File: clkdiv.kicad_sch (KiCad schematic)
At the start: 58 parts, among them J1 Conn_02x05_Odd_Even, J10 Conn_01x03_Pin, J11 Conn_01x03_Socket, J12 Conn_01x03_Pin, J13 Conn_01x03_Socket, J14 Conn_01x03_Pin, J15 Conn_01x03_Socket, J2 AudioJack2_SwitchT, J3 AudioJack2_SwitchT, J4 AudioJack2_SwitchT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

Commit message: fixes after prototyping
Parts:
- C4: value 1n box -> 47n box
- R11: value 22K -> 220K
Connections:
- net at R13.2: now also U1.7 (Q1); no longer U1.9 (Q0)
- net at R17.1: now also U1.2 (Q5); no longer U1.3 (Q4)
- net at R15.2: now also U1.5 (Q3); no longer U1.6 (Q2)
- net at R16.1: now also U1.3 (Q4); no longer U1.5 (Q3)
- net at R18.1: now also U1.4 (Q6); no longer U1.2 (Q5)
- net at R14.2: now also U1.6 (Q2); no longer U1.7 (Q1)
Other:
- moved on the sheet: R13, R14, R15, R16, R17, R18

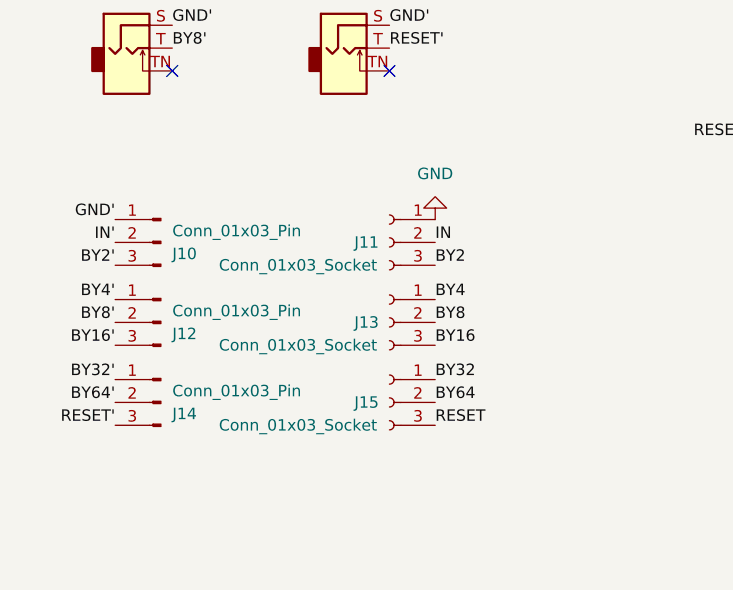
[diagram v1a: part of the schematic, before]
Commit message: pcb laid out, bom generated
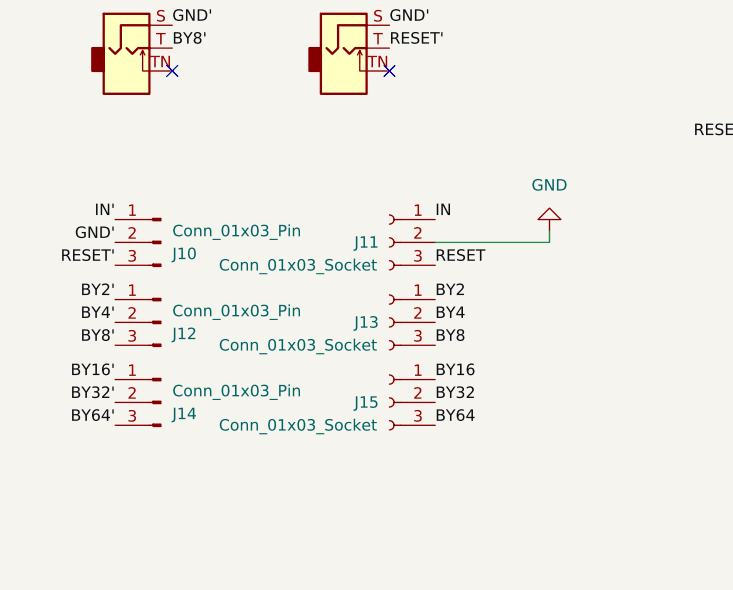
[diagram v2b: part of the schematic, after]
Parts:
- C3: footprint (none) -> Capacitor_SMD:C_0805_2012Metric
- C4: footprint (none) -> Capacitor_THT:C_Rect_L7.2mm_W2.5mm_P5.00mm_FKS2_FKP2_MKS2_MKP2
- D3, D4, D5: footprint (none) -> Diode_SMD:D_SOD-323_HandSoldering
- H10, H11, H6, H7, H8, H9: footprint Eurorack:Mech-MountingHole -> Eurorack:Mech-AudioJack-Hole-Output-Clock
- H12: footprint Eurorack:Mech-MountingHole -> Eurorack:Mech-AudioJack-Hole-Input-Gate
- H5: footprint Eurorack:Mech-MountingHole -> Eurorack:Mech-AudioJack-Hole-Input-Clock
- J10, J12, J14: footprint (none) -> Connector_PinHeader_2.54mm:PinHeader_1x03_P2.54mm_Vertical
- J11, J13, J15: footprint (none) -> Connector_PinSocket_2.54mm:PinSocket_1x03_P2.54mm_Vertical
- J2, J3, J4, J5, J6, J7, J8, J9: footprint (none) -> Eurorack:AudioJack2_Tayda_A-2566
- Q3, Q4: footprint (none) -> Package_SO:TSOP-6_1.65x3.05mm_P0.95mm; PartNum (none) -> 771-BCM847DS135; Vendor (none) -> Mouser
- R10, R11, R12, R13, R14, R15, R16, R17, R18, R19, R3, R4, R5, R6, R7, R8, R9: footprint (none) -> Resistor_SMD:R_0805_2012Metric
- U1: footprint (none) -> Package_SO:TSSOP-16_4.4x5mm_P0.65mm; PartNum (none) -> 595-CD4040BPWR; Vendor (none) -> Mouser
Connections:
- net BY16: now also J15.1 (Pin_1); no longer J13.3 (Pin_3)
- net BY16': now also J14.1 (Pin_1); no longer J12.3 (Pin_3)
- net BY2: now also J13.1 (Pin_1); no longer J11.3 (Pin_3)
- net BY2': now also J12.1 (Pin_1); no longer J10.3 (Pin_3)
- net BY32: now also J15.2 (Pin_2); no longer J15.1 (Pin_1)
- net BY32': now also J14.2 (Pin_2); no longer J14.1 (Pin_1)
- net BY4: now also J13.2 (Pin_2); no longer J13.1 (Pin_1)
- net BY4': now also J12.2 (Pin_2); no longer J12.1 (Pin_1)
- net BY64: now also J15.3 (Pin_3); no longer J15.2 (Pin_2)
- net BY64': now also J14.3 (Pin_3); no longer J14.2 (Pin_2)
- net BY8: now also J13.3 (Pin_3); no longer J13.2 (Pin_2)
- net BY8': now also J12.3 (Pin_3); no longer J12.2 (Pin_2)
- net GND: now also J11.2 (Pin_2); no longer J11.1 (Pin_1)
- net GND': now also J10.2 (Pin_2); no longer J10.1 (Pin_1)
- net IN: now also J11.1 (Pin_1); no longer J11.2 (Pin_2)
- net IN': now also J10.1 (Pin_1); no longer J10.2 (Pin_2)
- net RESET: now also J11.3 (Pin_3); no longer J15.3 (Pin_3)
- net RESET': now also J10.3 (Pin_3); no longer J14.3 (Pin_3)
